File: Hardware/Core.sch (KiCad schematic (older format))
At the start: 24 parts

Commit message: Prepare for new core
Clear core subsheet
Remove expansion
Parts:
- removed C?: DNP, CAPC1005-N, symbol C
- removed C? (x2): 4.7uF, CAPC2012-N, symbol C
- removed C? (x2): 22pF, CAPC1005-N, symbol C
- removed C? (x2): 0.1uF, CAPC1005-N, symbol C
- removed C? (x4): 1200pF, CAPC1005-N, symbol C
- removed L?: 4.7uH, INDC3225-N, symbol L
- removed R? (x7): 10k, RESC1005-N, symbol R
- removed U?: AAT1217, symbol AAT1217
- removed U? (x2): MCP6L02T, SOP65P490-8N, symbol OPAMP-DUAL
- removed U?: MSP430G2553-PW28, symbol MSP430G2553-PW28
- removed X?: 8MHz, XTAL-2SMD-50X32, symbol CRYSTAL
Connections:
- net labels removed: +3.3V, +BATT, AF, CLK_En, E1, E2, GND, GPS_En, GPS_Perf, Lx, MOSI, Mod, PGM_Det, RX, SCK, SCL, SDA, SS, Stat, TCK/TEST, TDIO/RST, TX, TXD, TX_En, XIn, XOut
- wire segments 86 -> 0
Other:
- note removed: "Butterworth LPF"

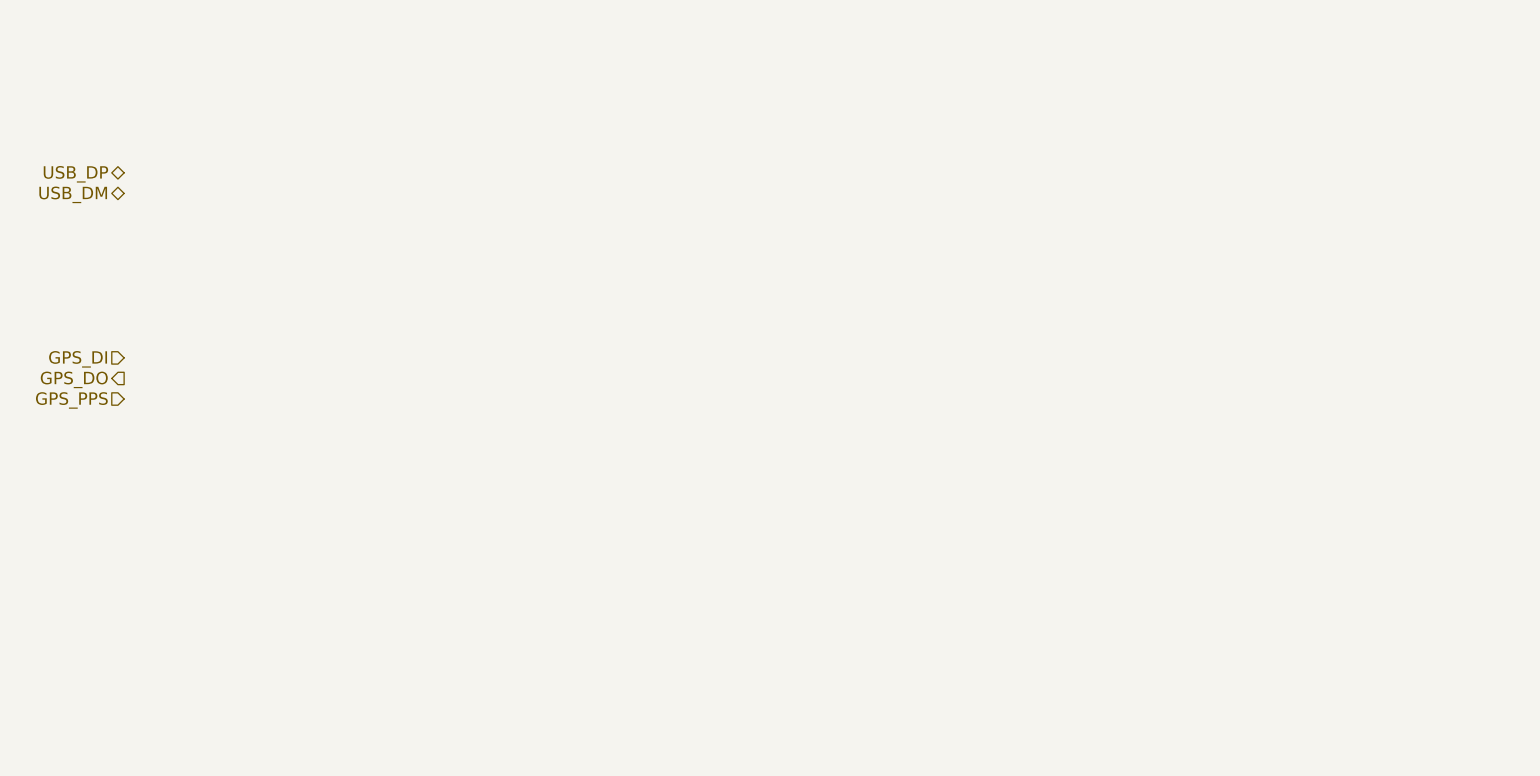
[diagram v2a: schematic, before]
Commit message: Add STM32L100
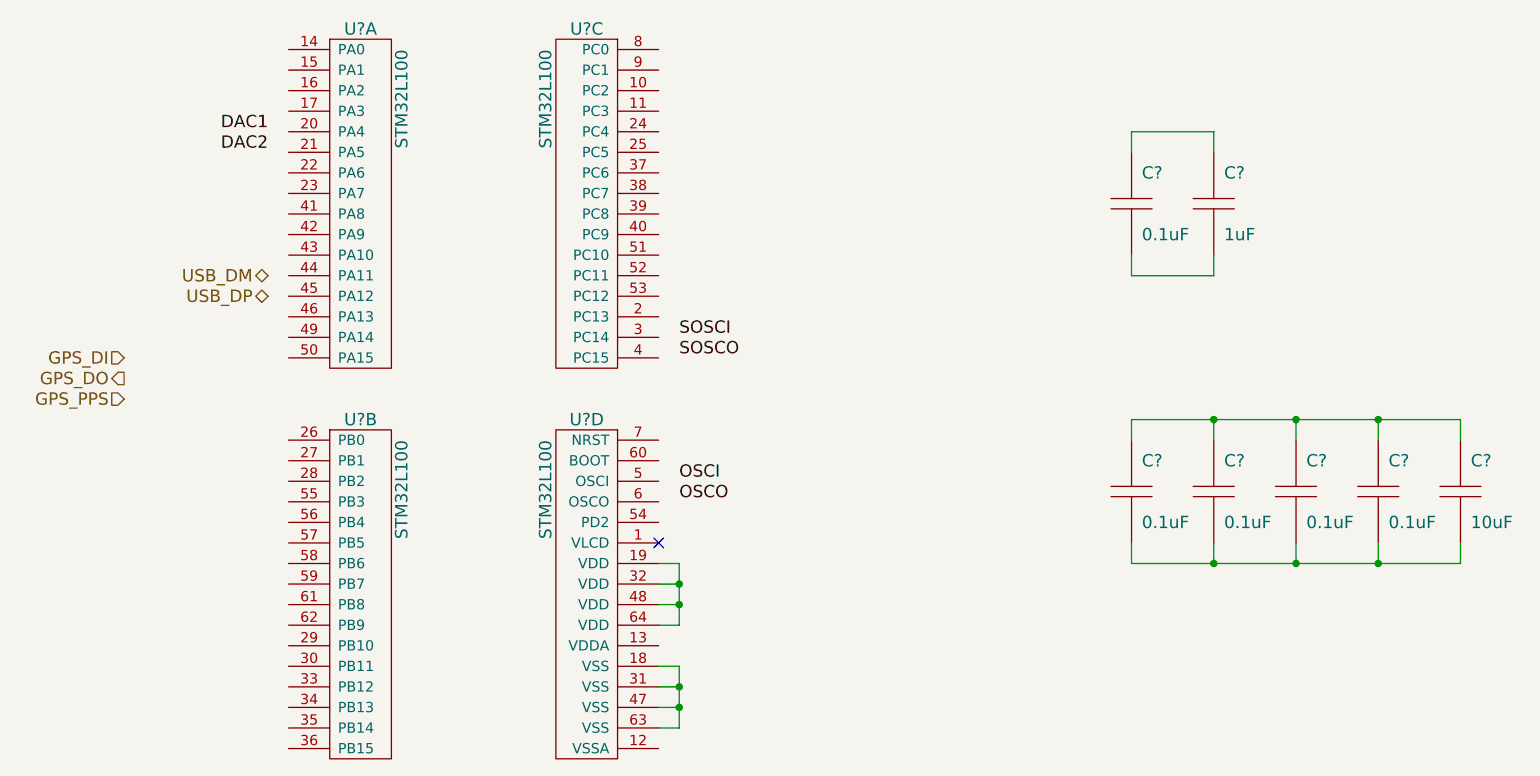
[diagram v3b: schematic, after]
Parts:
- added C? (x5): 0.1uF, ~, symbol C
- added C?: 1uF, ~, symbol C
- added C?: 10uF, ~, symbol C
- added U? (x4): STM32L100, symbol STM32L100
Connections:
- new net: U?.18 (VSS), U?.31 (VSS), U?.47 (VSS), U?.63 (VSS)
- new net: U?.19 (VDD), U?.32 (VDD), U?.48 (VDD), U?.64 (VDD)
- new net: C?.1, C?.1
- new net: C?.2, C?.2
- new net: C?.1, C?.1, C?.1, C?.1, C?.1
- new net: C?.2, C?.2, C?.2, C?.2, C?.2
- no-connect marks 0 -> 1
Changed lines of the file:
@@
 Sheet 3 4
 Title "Aether - Pico Tracker"
-Date "29 jun 2014"
+Date "29 jul 2014"
 Rev "1"
 Comp "Aerodyne Labs"
@@
 Text HLabel 4100 3300 0    60   Input ~ 0
 GPS_PPS
-Text HLabel 4100 2200 0    60   BiDi ~ 0
+Text HLabel 4800 2800 0    60   BiDi ~ 0
 USB_DP
-Text HLabel 4100 2300 0    60   BiDi ~ 0
+Text HLabel 4800 2700 0    60   BiDi ~ 0
 USB_DM
+$Comp
+L STM32L100 U?
+U 1 1 53D70C95
+P 5250 1600
+F 0 "U?" H 5250 1700 60  0000 C CNN
+F 1 "STM32L100" V 5050 1600 60  0000 R CNN
+F 2 "" H 5250 1600 60  0000 C CNN
+F 3 "" H 5250 1600 60  0000 C CNN
+	1    5250 1600
+	-1   0    0    -1
+$EndComp
+$Comp
+L STM32L100 U?
+U 2 1 53D70CA4
+P 5250 3500
+F 0 "U?" H 5250 3600 60  0000 C CNN
+F 1 "STM32L100" V 5050 3500 60  0000 R CNN
+F 2 "" H 5250 3500 60  0000 C CNN
+F 3 "" H 5250 3500 60  0000 C CNN
+	2    5250 3500
+	-1   0    0    -1
+$EndComp
+$Comp
+L STM32L100 U?
+U 3 1 53D70CB3
+P 6350 1600
+F 0 "U?" H 6350 1700 60  0000 C CNN
+F 1 "STM32L100" V 6150 1600 60  0000 R CNN
+F 2 "" H 6350 1600 60  0000 C CNN
+F 3 "" H 6350 1600 60  0000 C CNN
+	3    6350 1600
+	1    0    0    -1
+$EndComp
+$Comp
+L STM32L100 U?
+U 4 1 53D70CC2
+P 6350 3500
+F 0 "U?" H 6350 3600 60  0000 C CNN
+F 1 "STM32L100" V 6150 3500 60  0000 R CNN
+F 2 "" H 6350 3500 60  0000 C CNN
+F 3 "" H 6350 3500 60  0000 C CNN
+	4    6350 3500
+	1    0    0    -1
+$EndComp
+Text Label 6800 3000 0    60   ~ 0
+SOSCI
+Text Label 6800 3100 0    60   ~ 0
+SOSCO
+Text Label 6800 3700 0    60   ~ 0
+OSCI
+Text Label 6800 3800 0    60   ~ 0
+OSCO
+Text Label 4800 2000 2    60   ~ 0
+DAC1
+Text Label 4800 2100 2    60   ~ 0
+DAC2
+$Comp
+L C C?
+U 1 1 53D70CF0
+P 9000 2350
+F 0 "C?" H 9050 2500 60  0000 L CNN
+F 1 "0.1uF" H 9050 2200 60  0000 L CNN
+F 2 "~" H 9000 2350 60  0000 C CNN
+F 3 "~" H 9000 2350 60  0000 C CNN
+F 4 "V" H 8950 2200 60  0001 R CNN "Voltage"
+F 5 "D" H 8950 2500 60  0001 R CNN "Dielectric"
+	1    9000 2350
+	1    0    0    -1
+$EndComp
+$Comp
+L C C?
+U 1 1 53D70D12
+P 9400 2350
+F 0 "C?" H 9450 2500 60  0000 L CNN
+F 1 "1uF" H 9450 2200 60  0000 L CNN
+F 2 "~" H 9400 2350 60  0000 C CNN
+F 3 "~" H 9400 2350 60  0000 C CNN
+F 4 "V" H 9350 2200 60  0001 R CNN "Voltage"
+F 5 "D" H 9350 2500 60  0001 R CNN "Dielectric"
+	1    9400 2350
+	1    0    0    -1
+$EndComp
+$Comp
+L C C?
+U 1 1 53D70D3B
+P 9000 3750
+F 0 "C?" H 9050 3900 60  0000 L CNN
+F 1 "0.1uF" H 9050 3600 60  0000 L CNN
+F 2 "~" H 9000 3750 60  0000 C CNN
+F 3 "~" H 9000 3750 60  0000 C CNN
+F 4 "V" H 8950 3600 60  0001 R CNN "Voltage"
+F 5 "D" H 8950 3900 60  0001 R CNN "Dielectric"
+	1    9000 3750
+	1    0    0    -1
+$EndComp
+$Comp
+L C C?
+U 1 1 53D70D43
+P 9400 3750
+F 0 "C?" H 9450 3900 60  0000 L CNN
+F 1 "0.1uF" H 9450 3600 60  0000 L CNN
+F 2 "~" H 9400 3750 60  0000 C CNN
+F 3 "~" H 9400 3750 60  0000 C CNN
+F 4 "V" H 9350 3600 60  0001 R CNN "Voltage"
+F 5 "D" H 9350 3900 60  0001 R CNN "Dielectric"
+	1    9400 3750
+	1    0    0    -1
+$EndComp
+$Comp
+L C C?
+U 1 1 53D70D4B
+P 9800 3750
+F 0 "C?" H 9850 3900 60  0000 L CNN
+F 1 "0.1uF" H 9850 3600 60  0000 L CNN
+F 2 "~" H 9800 3750 60  0000 C CNN
+F 3 "~" H 9800 3750 60  0000 C CNN
+F 4 "V" H 9750 3600 60  0001 R CNN "Voltage"
+F 5 "D" H 9750 3900 60  0001 R CNN "Dielectric"
+	1    9800 3750
+	1    0    0    -1
+$EndComp
+$Comp
+L C C?
+U 1 1 53D70D53
+P 10200 3750
+F 0 "C?" H 10250 3900 60  0000 L CNN
+F 1 "0.1uF" H 10250 3600 60  0000 L CNN
+F 2 "~" H 10200 3750 60  0000 C CNN
+F 3 "~" H 10200 3750 60  0000 C CNN
+F 4 "V" H 10150 3600 60  0001 R CNN "Voltage"
+F 5 "D" H 10150 3900 60  0001 R CNN "Dielectric"
+	1    10200 3750
+	1    0    0    -1
+$EndComp
+$Comp
+L C C?
+U 1 1 53D70D5B
+P 10600 3750
+F 0 "C?" H 10650 3900 60  0000 L CNN
+F 1 "10uF" H 10650 3600 60  0000 L CNN
+F 2 "~" H 10600 3750 60  0000 C CNN
+F 3 "~" H 10600 3750 60  0000 C CNN
+F 4 "V" H 10550 3600 60  0001 R CNN "Voltage"
+F 5 "D" H 10550 3900 60  0001 R CNN "Dielectric"
+	1    10600 3750
+	1    0    0    -1
+$EndComp
+Wire Wire Line
+	9000 3500 9000 3400
+Wire Wire Line
+	9000 3400 10600 3400
+Wire Wire Line
+	10600 3400 10600 3500
+Wire Wire Line
+	9000 2100 9000 2000
+Wire Wire Line
+	9000 2000 9400 2000
+Wire Wire Line
+	9400 2000 9400 2100
+Wire Wire Line
+	6700 4100 6800 4100
+Wire Wire Line
+	6800 4100 6800 4400
+Wire Wire Line
+	6800 4400 6700 4400
+Wire Wire Line
+	6700 4200 6800 4200
+Connection ~ 6800 4200
+Wire Wire Line
+	6700 4300 6800 4300
+Connection ~ 6800 4300
+Wire Wire Line
+	6700 4600 6800 4600
+Wire Wire Line
+	6800 4600 6800 4900
+Wire Wire Line
+	6800 4900 6700 4900
+Wire Wire Line
+	6700 4700 6800 4700
+Connection ~ 6800 4700
+Wire Wire Line
+	6700 4800 6800 4800
+Connection ~ 6800 4800
+NoConn ~ 6700 4000
+Wire Wire Line
+	9400 3500 9400 3400
+Connection ~ 9400 3400
+Wire Wire Line
+	9800 3500 9800 3400
+Connection ~ 9800 3400
+Wire Wire Line
+	10200 3500 10200 3400
+Connection ~ 10200 3400
+Wire Wire Line
+	9000 4000 9000 4100
+Wire Wire Line
+	9000 4100 10600 4100
+Wire Wire Line
+	10600 4100 10600 4000
+Wire Wire Line
+	10200 4000 10200 4100
+Connection ~ 10200 4100
+Wire Wire Line
+	9800 4000 9800 4100
+Connection ~ 9800 4100
+Wire Wire Line
+	9400 4000 9400 4100
+Connection ~ 9400 4100
+Wire Wire Line
+	9000 2600 9000 2700
+Wire Wire Line
+	9000 2700 9400 2700
+Wire Wire Line
+	9400 2700 9400 2600
 $EndSCHEMATC

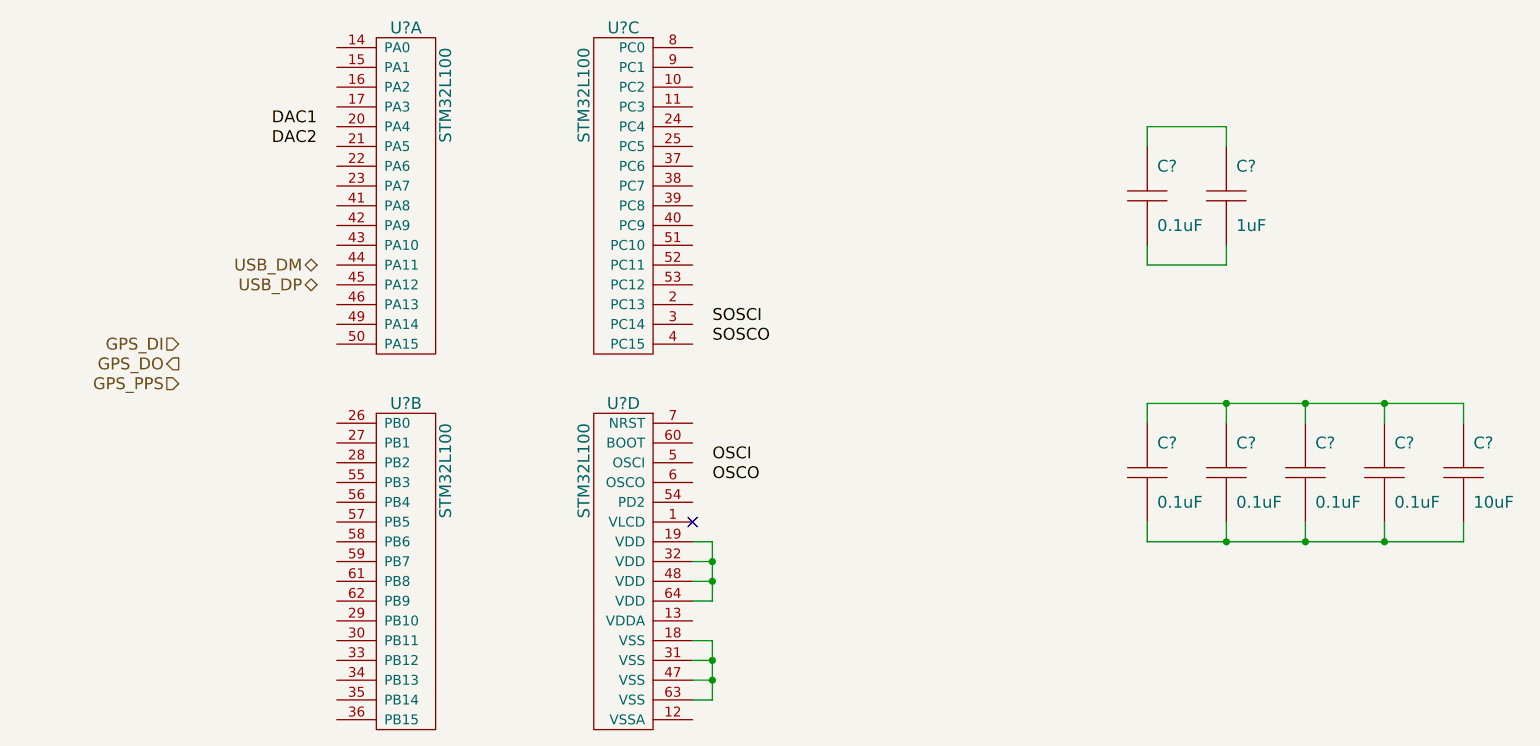
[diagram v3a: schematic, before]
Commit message: Core pin placeholders
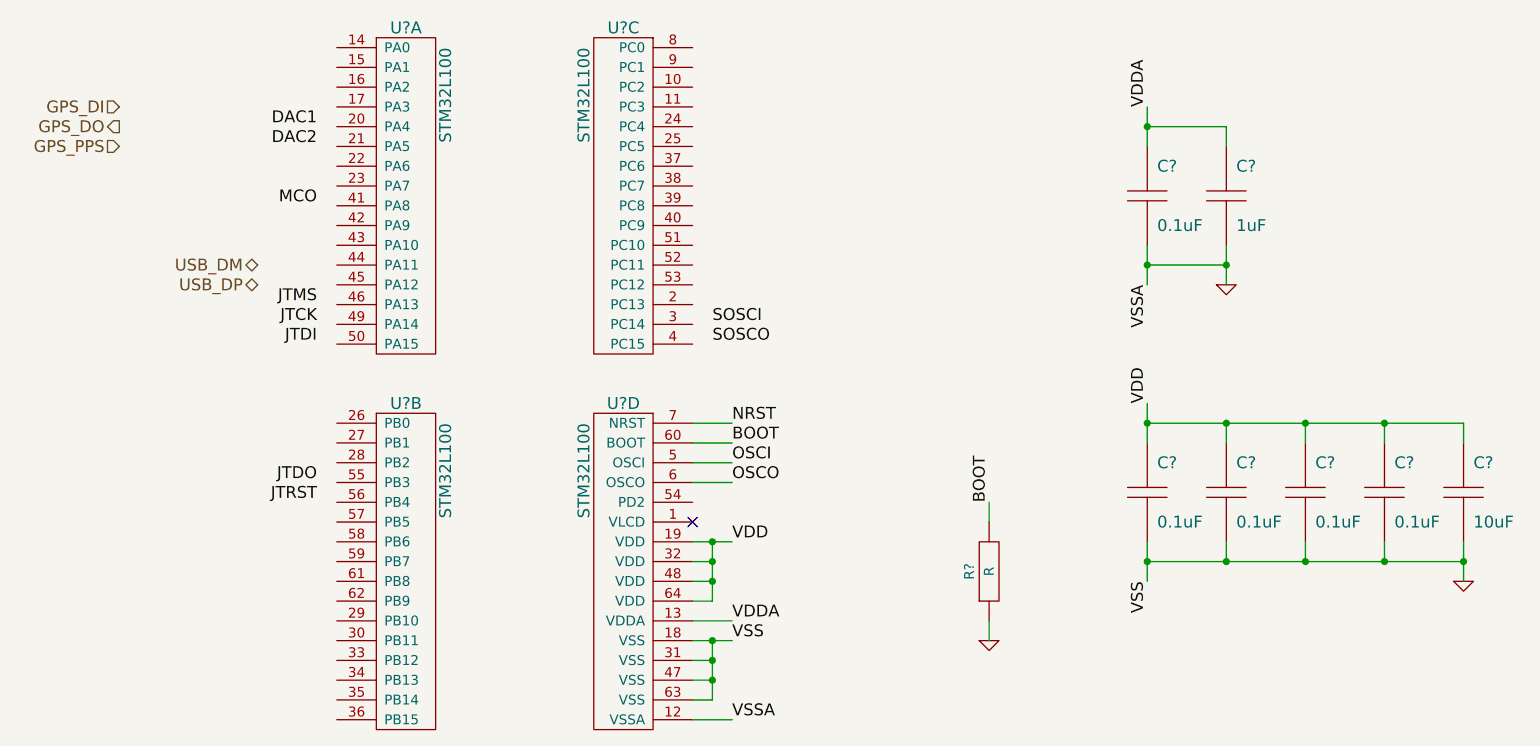
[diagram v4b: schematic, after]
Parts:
- added R?: R, ~, symbol R
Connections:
- net OSCI: now also U?.5 (OSCI)
- net OSCO: now also U?.6 (OSCO)
- net GND: now reaches U?.12 (VSSA)
- net GND: now also C?.2, C?.2, C?.2, C?.2, C?.2, C?.2, C?.2, U?.18 (VSS), U?.31 (VSS), U?.47 (VSS), U?.63 (VSS), R?.1
- net VDDA: now reaches U?.13 (VDDA)
- net VDDA: now also C?.1, C?.1
- net VDD: now reaches U?.19 (VDD), U?.32 (VDD), U?.48 (VDD), U?.64 (VDD)
- net VDD: now also C?.1, C?.1, C?.1, C?.1, C?.1
- net BOOT: now reaches U?.60 (BOOT)
- net BOOT: now also R?.2
- net NRST: now reaches U?.7 (NRST)
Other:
- moved on the sheet: C?
